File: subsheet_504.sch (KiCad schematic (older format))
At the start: 36 parts, among them J502 Phono LEFT, J503 Phono RIGHT, U504 LF347N_mu, U508 LMC1992CCN_PHY

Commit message: Removed T-filters
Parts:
- removed L504, L505: EMI_Filter_LCL, commons_passives_THT:Passive_THT_EMI_filter_W5.08mm_L7.62mm, symbol Device:EMI_Filter_LCL
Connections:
- wire segments 108 -> 106
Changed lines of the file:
@@
 $EndComp
-$Comp
-L Device:EMI_Filter_LCL L?
-U 1 1 60D98994
-P 1650 6750
-AR Path="/608A2359/60D98994" Ref="L?"  Part="1"
-AR Path="/608C2344/60D98994" Ref="L?"  Part="1"
-AR Path="/608EA3C9/60D98994" Ref="L?"  Part="1"
-AR Path="/609B5A51/60D98994" Ref="L?"  Part="1"
-AR Path="/60B3D9E3/60D98994" Ref="L?"  Part="1"
-AR Path="/60CD36E9/60D98994" Ref="L504"  Part="1"
-F 0 "L504" V 1750 6450 50  0000 C CNN
-F 1 "EMI_Filter_LCL" V 1850 6450 50  0000 C CNN
-F 2 "commons_passives_THT:Passive_THT_EMI_filter_W5.08mm_L7.62mm" V 1650 6750 50  0001 C CNN
-F 3 "http://www.murata.com/~/media/webrenewal/support/library/catalog/products/emc/emifil/c31e.ashx?la=en-gb" V 1650 6750 50  0001 C CNN
-	1    1650 6750
-	0    1    1    0
-$EndComp
-Text Label 1550 6750 2    50   ~ 0
-GND
 $Comp
 L Device:R_Small_US R?
@@
 Wire Wire Line
 	1750 5600 1750 5850
-Wire Wire Line
-	1750 6150 1750 6450
-Wire Wire Line
-	1750 7050 1750 7500
 Wire Wire Line
 	1600 7500 1750 7500
@@
 $EndComp
 $Comp
-L Device:EMI_Filter_LCL L?
-U 1 1 60DBE194
-P 6400 6750
-AR Path="/608A2359/60DBE194" Ref="L?"  Part="1"
-AR Path="/608C2344/60DBE194" Ref="L?"  Part="1"
-AR Path="/608EA3C9/60DBE194" Ref="L?"  Part="1"
-AR Path="/609B5A51/60DBE194" Ref="L?"  Part="1"
-AR Path="/60B3D9E3/60DBE194" Ref="L?"  Part="1"
-AR Path="/60CD36E9/60DBE194" Ref="L505"  Part="1"
-F 0 "L505" V 6500 6450 50  0000 C CNN
-F 1 "EMI_Filter_LCL" V 6600 6450 50  0000 C CNN
-F 2 "commons_passives_THT:Passive_THT_EMI_filter_W5.08mm_L7.62mm" V 6400 6750 50  0001 C CNN
-F 3 "http://www.murata.com/~/media/webrenewal/support/library/catalog/products/emc/emifil/c31e.ashx?la=en-gb" V 6400 6750 50  0001 C CNN
-	1    6400 6750
-	0    1    1    0
-$EndComp
-Text Label 6300 6750 2    50   ~ 0
-GND
-$Comp
 L Device:R_Small_US R?
 U 1 1 60DBE19B
@@
 Wire Wire Line
 	6500 5600 6500 5850
-Wire Wire Line
-	6500 6150 6500 6450
-Wire Wire Line
-	6500 7050 6500 7500
 Wire Wire Line
 	6350 7500 6500 7500
@@
 Wire Notes Line
 	5150 2400 7650 2400
+Wire Wire Line
+	1750 6150 1750 7500
+Wire Wire Line
+	6500 6150 6500 7500
 $EndSCHEMATC

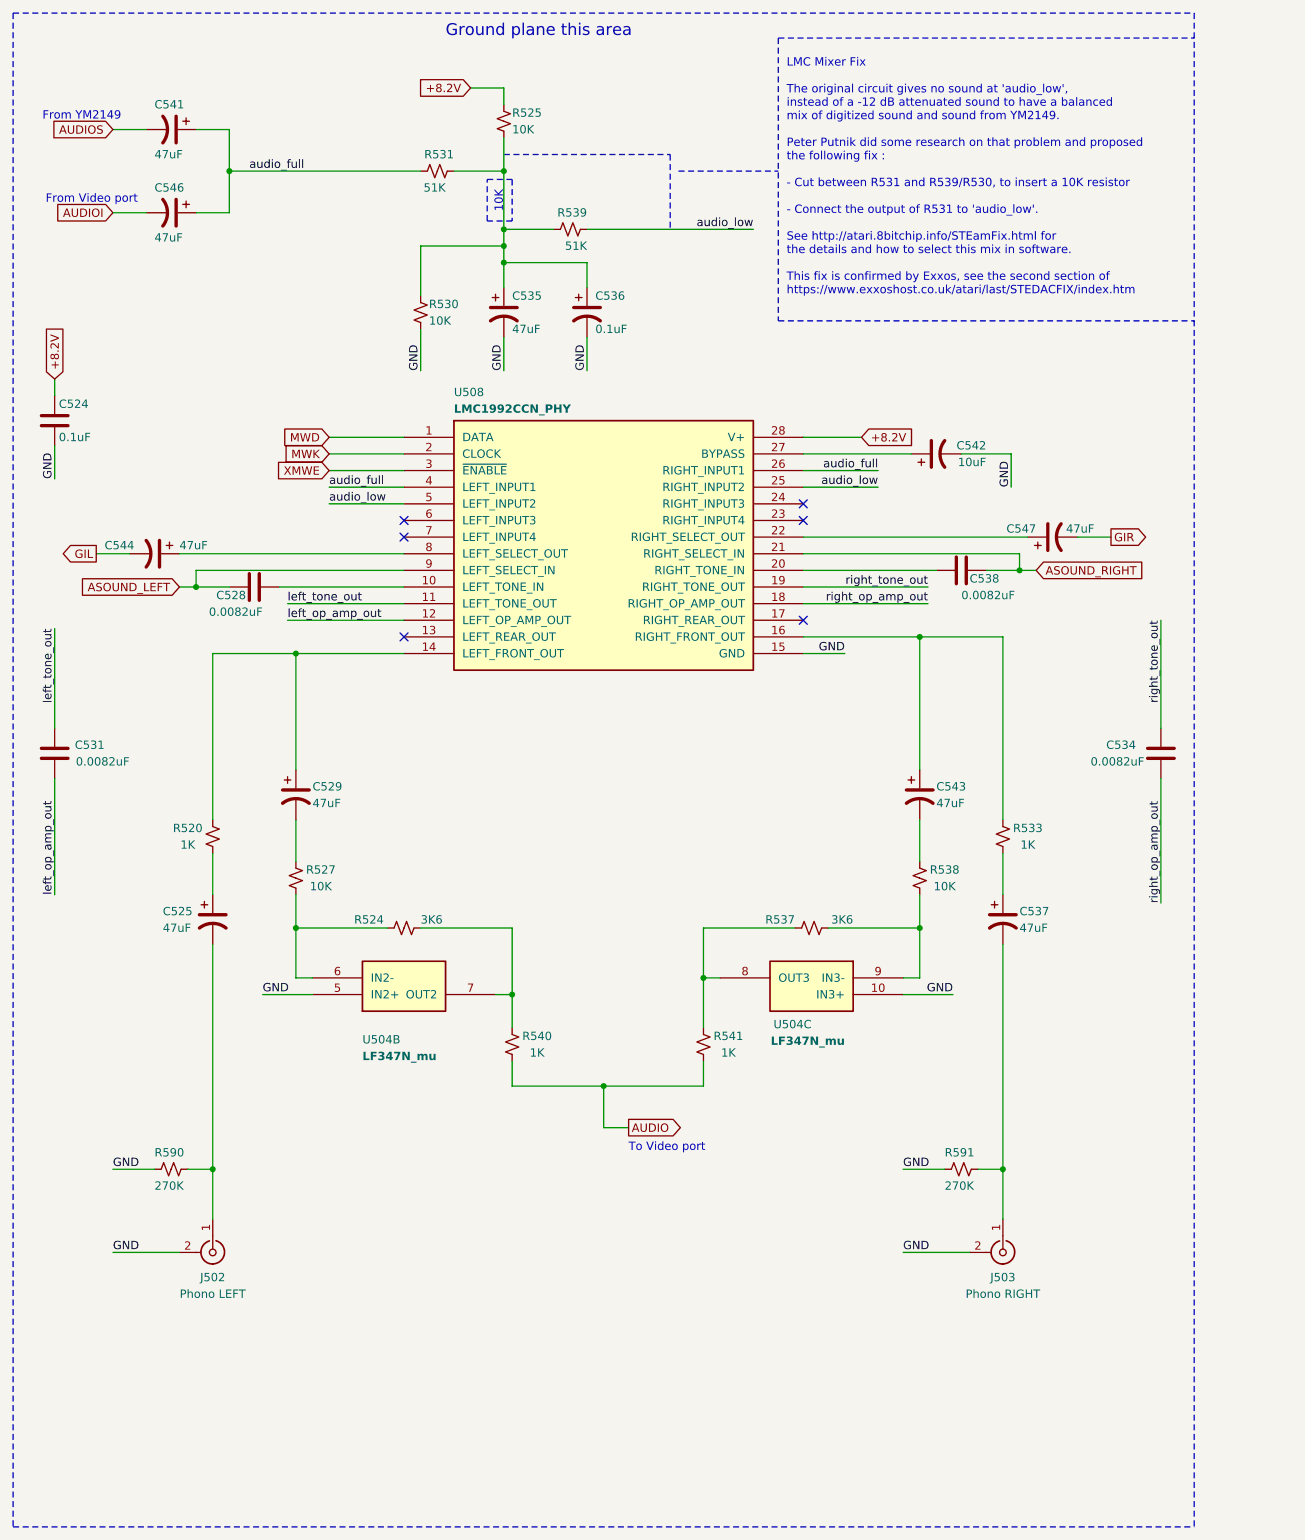
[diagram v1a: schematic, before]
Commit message: Resolves #12 : Use the reference 'CP?' for polarized capacitors
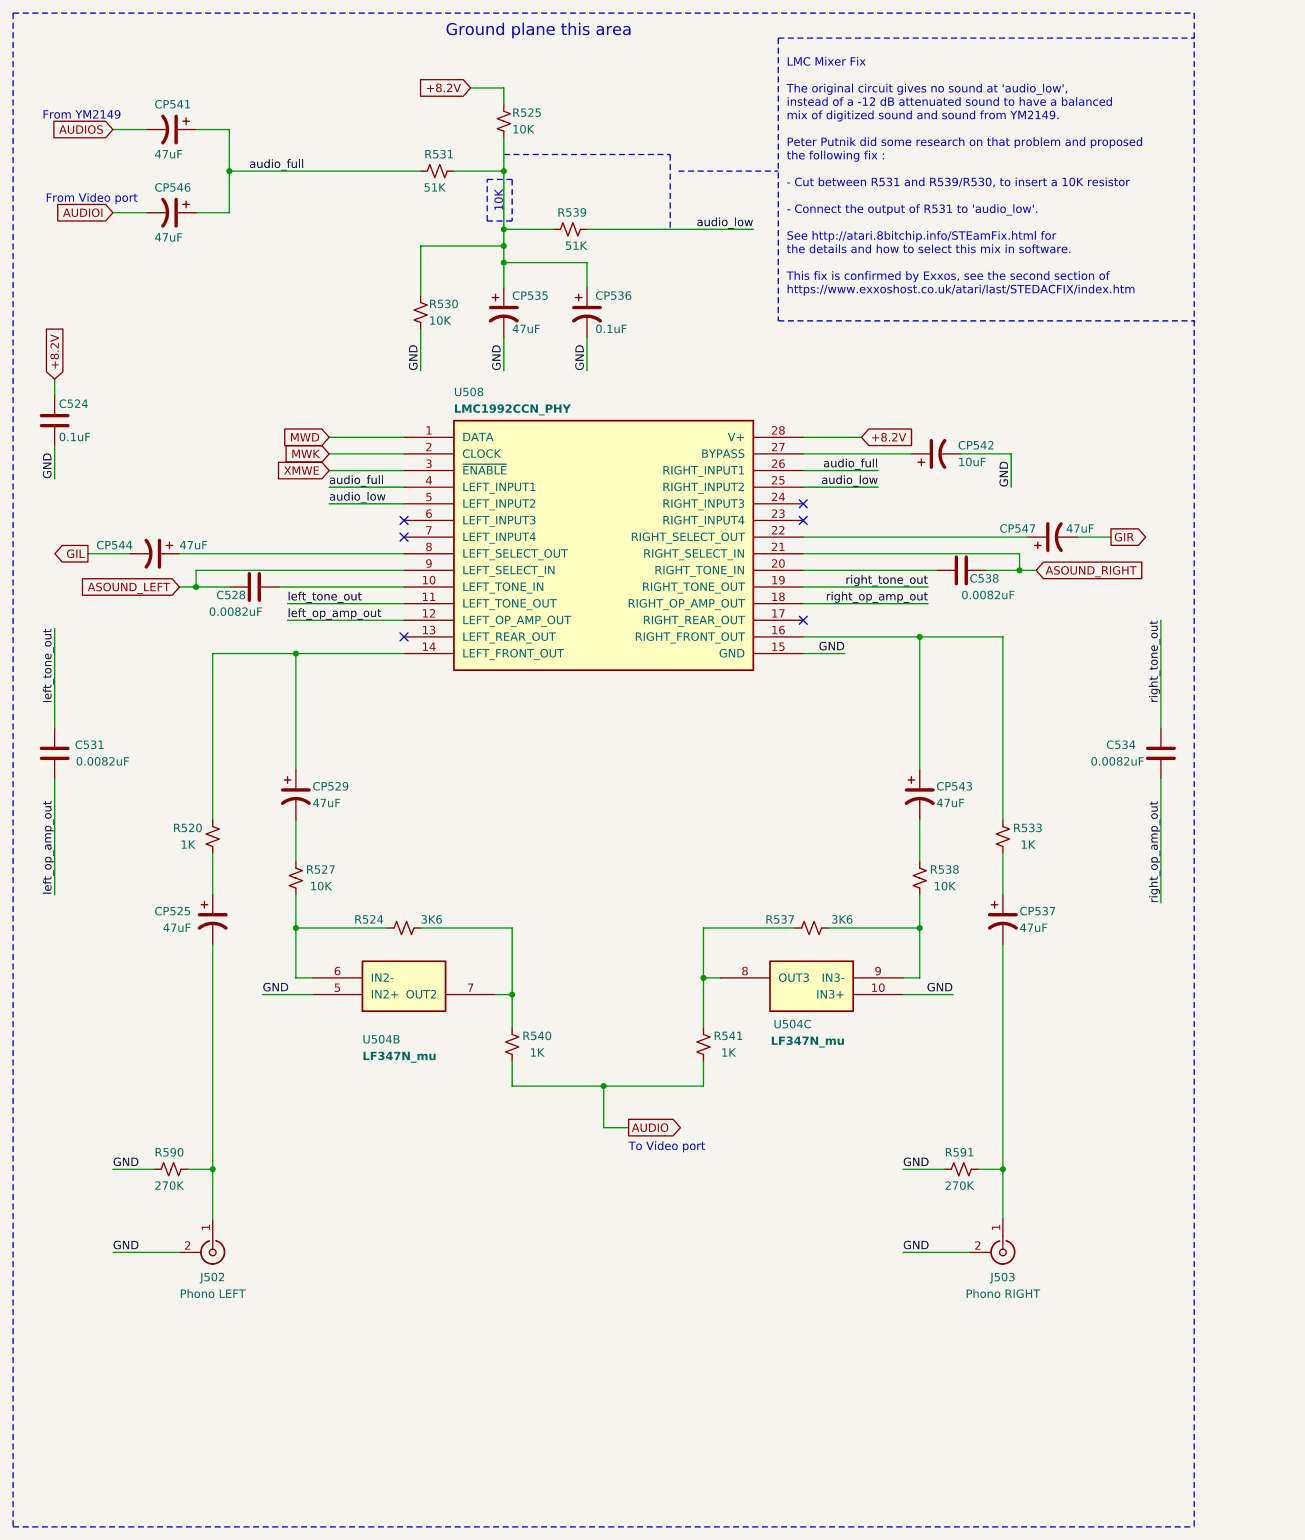
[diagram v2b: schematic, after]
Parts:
- renumbered C525 to CP525, C529 to CP529, C535 to CP535, C536 to CP536, C537 to CP537, C541 to CP541, C542 to CP542, C543 to CP543, C544 to CP544, C546 to CP546, C547 to CP547
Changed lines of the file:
@@
 Text GLabel 7150 3700 2    50   Output ~ 0
 GIR
-Text GLabel 1050 3800 0    50   Output ~ 0
+Text GLabel 1000 3800 0    50   Output ~ 0
 GIL
 Text GLabel 1150 1250 0    50   Input ~ 0
@@
 AR Path="/60C95DE8/60CED58A" Ref="C?"  Part="1"
 AR Path="/60CC3B10/60CED58A" Ref="C?"  Part="1"
-AR Path="/60CD36E9/60CED58A" Ref="C535"  Part="1"
-F 0 "C535" H 3550 2450 50  0000 L CNN
+AR Path="/60CD36E9/60CED58A" Ref="CP535"  Part="1"
+F 0 "CP535" H 3550 2450 50  0000 L CNN
 F 1 "47uF" H 3550 2250 50  0000 L CNN
 F 2 "commons_passives_THT:Passive_THT_capacitor_polarized_W6.35mm_L20.32mm" H 3500 2350 50  0001 C CNN
@@
 AR Path="/60C95DE8/60CEE43A" Ref="C?"  Part="1"
 AR Path="/60CC3B10/60CEE43A" Ref="C?"  Part="1"
-AR Path="/60CD36E9/60CEE43A" Ref="C536"  Part="1"
-F 0 "C536" H 4050 2450 50  0000 L CNN
+AR Path="/60CD36E9/60CEE43A" Ref="CP536"  Part="1"
+F 0 "CP536" H 4050 2450 50  0000 L CNN
 F 1 "0.1uF" H 4050 2250 50  0000 L CNN
 F 2 "commons_passives_THT:Passive_THT_capacitor_mlcc_W2.54mm_L7.62mm" H 4000 2350 50  0001 C CNN
@@
 AR Path="/60C95DE8/60CF0999" Ref="C?"  Part="1"
 AR Path="/60CC3B10/60CF0999" Ref="C?"  Part="1"
-AR Path="/60CD36E9/60CF0999" Ref="C541"  Part="1"
-F 0 "C541" V 1350 1150 50  0000 L CNN
+AR Path="/60CD36E9/60CF0999" Ref="CP541"  Part="1"
+F 0 "CP541" V 1350 1150 50  0000 L CNN
 F 1 "47uF" V 1650 1150 50  0000 L CNN
 F 2 "commons_passives_THT:Passive_THT_capacitor_polarized_W6.35mm_L20.32mm" H 1500 1250 50  0001 C CNN
@@
 AR Path="/60C95DE8/60CF36CC" Ref="C?"  Part="1"
 AR Path="/60CC3B10/60CF36CC" Ref="C?"  Part="1"
-AR Path="/60CD36E9/60CF36CC" Ref="C546"  Part="1"
-F 0 "C546" V 1350 1650 50  0000 L CNN
+AR Path="/60CD36E9/60CF36CC" Ref="CP546"  Part="1"
+F 0 "CP546" V 1350 1650 50  0000 L CNN
 F 1 "47uF" V 1650 1650 50  0000 L CNN
 F 2 "commons_passives_THT:Passive_THT_capacitor_polarized_W6.35mm_L20.32mm" H 1500 1750 50  0001 C CNN
@@
 AR Path="/60C95DE8/60CF439B" Ref="C?"  Part="1"
 AR Path="/60CC3B10/60CF439B" Ref="C?"  Part="1"
-AR Path="/60CD36E9/60CF439B" Ref="C544"  Part="1"
-F 0 "C544" V 1350 3500 50  0000 L CNN
+AR Path="/60CD36E9/60CF439B" Ref="CP544"  Part="1"
+F 0 "CP544" V 1350 3450 50  0000 L CNN
 F 1 "47uF" V 1350 3950 50  0000 L CNN
 F 2 "commons_passives_THT:Passive_THT_capacitor_polarized_W6.35mm_L20.32mm" H 1400 3800 50  0001 C CNN
@@
 	0    1    1    0
 $EndComp
-Wire Wire Line
-	1050 3800 1250 3800
 $Comp
 L Device:CP1 C?
@@
 AR Path="/60C95DE8/60CF5477" Ref="C?"  Part="1"
 AR Path="/60CC3B10/60CF5477" Ref="C?"  Part="1"
-AR Path="/60CD36E9/60CF5477" Ref="C547"  Part="1"
-F 0 "C547" V 6850 3800 50  0000 L CNN
+AR Path="/60CD36E9/60CF5477" Ref="CP547"  Part="1"
+F 0 "CP547" V 6850 3800 50  0000 L CNN
 F 1 "47uF" V 6850 3450 50  0000 L CNN
 F 2 "commons_passives_THT:Passive_THT_capacitor_polarized_W6.35mm_L20.32mm" H 6800 3700 50  0001 C CNN
@@
 AR Path="/60C95DE8/60D91985" Ref="C?"  Part="1"
 AR Path="/60CC3B10/60D91985" Ref="C?"  Part="1"
-AR Path="/60CD36E9/60D91985" Ref="C525"  Part="1"
-F 0 "C525" H 1450 6050 50  0000 L CNN
+AR Path="/60CD36E9/60D91985" Ref="CP525"  Part="1"
+F 0 "CP525" H 1400 6050 50  0000 L CNN
 F 1 "47uF" H 1450 5950 50  0000 L CNN
 F 2 "commons_passives_THT:Passive_THT_capacitor_polarized_W6.35mm_L20.32mm" H 1750 6000 50  0001 C CNN
@@
 AR Path="/60C95DE8/60DBE18E" Ref="C?"  Part="1"
 AR Path="/60CC3B10/60DBE18E" Ref="C?"  Part="1"
-AR Path="/60CD36E9/60DBE18E" Ref="C537"  Part="1"
-F 0 "C537" H 6600 6050 50  0000 L CNN
+AR Path="/60CD36E9/60DBE18E" Ref="CP537"  Part="1"
+F 0 "CP537" H 6600 6050 50  0000 L CNN
 F 1 "47uF" H 6600 5950 50  0000 L CNN
 F 2 "commons_passives_THT:Passive_THT_capacitor_polarized_W6.35mm_L20.32mm" H 6500 6000 50  0001 C CNN
@@
 AR Path="/60C95DE8/60DC0622" Ref="C?"  Part="1"
 AR Path="/60CC3B10/60DC0622" Ref="C?"  Part="1"
-AR Path="/60CD36E9/60DC0622" Ref="C529"  Part="1"
-F 0 "C529" H 2350 5300 50  0000 L CNN
+AR Path="/60CD36E9/60DC0622" Ref="CP529"  Part="1"
+F 0 "CP529" H 2350 5300 50  0000 L CNN
 F 1 "47uF" H 2350 5200 50  0000 L CNN
 F 2 "commons_passives_THT:Passive_THT_capacitor_polarized_W6.35mm_L20.32mm" H 2250 5250 50  0001 C CNN
@@
 AR Path="/60C95DE8/60DDE603" Ref="C?"  Part="1"
 AR Path="/60CC3B10/60DDE603" Ref="C?"  Part="1"
-AR Path="/60CD36E9/60DDE603" Ref="C543"  Part="1"
-F 0 "C543" H 6100 5300 50  0000 L CNN
+AR Path="/60CD36E9/60DDE603" Ref="CP543"  Part="1"
+F 0 "CP543" H 6100 5300 50  0000 L CNN
 F 1 "47uF" H 6100 5200 50  0000 L CNN
 F 2 "commons_passives_THT:Passive_THT_capacitor_polarized_W6.35mm_L20.32mm" H 6000 5250 50  0001 C CNN
@@
 AR Path="/60C95DE8/60E01C9D" Ref="C?"  Part="1"
 AR Path="/60CC3B10/60E01C9D" Ref="C?"  Part="1"
-AR Path="/60CD36E9/60E01C9D" Ref="C542"  Part="1"
-F 0 "C542" V 6150 2900 50  0000 L CNN
+AR Path="/60CD36E9/60E01C9D" Ref="CP542"  Part="1"
+F 0 "CP542" V 6150 2850 50  0000 L CNN
 F 1 "10uF" V 6050 2900 50  0000 L CNN
 F 2 "commons_passives_THT:Passive_THT_capacitor_polarized_W5.08mm_L17.78mm" H 6100 3200 50  0001 C CNN
@@
 Wire Wire Line
 	6500 6150 6500 7500
+Wire Wire Line
+	1000 3800 1250 3800
 $EndSCHEMATC
